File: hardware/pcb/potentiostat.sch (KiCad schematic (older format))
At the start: 58 parts

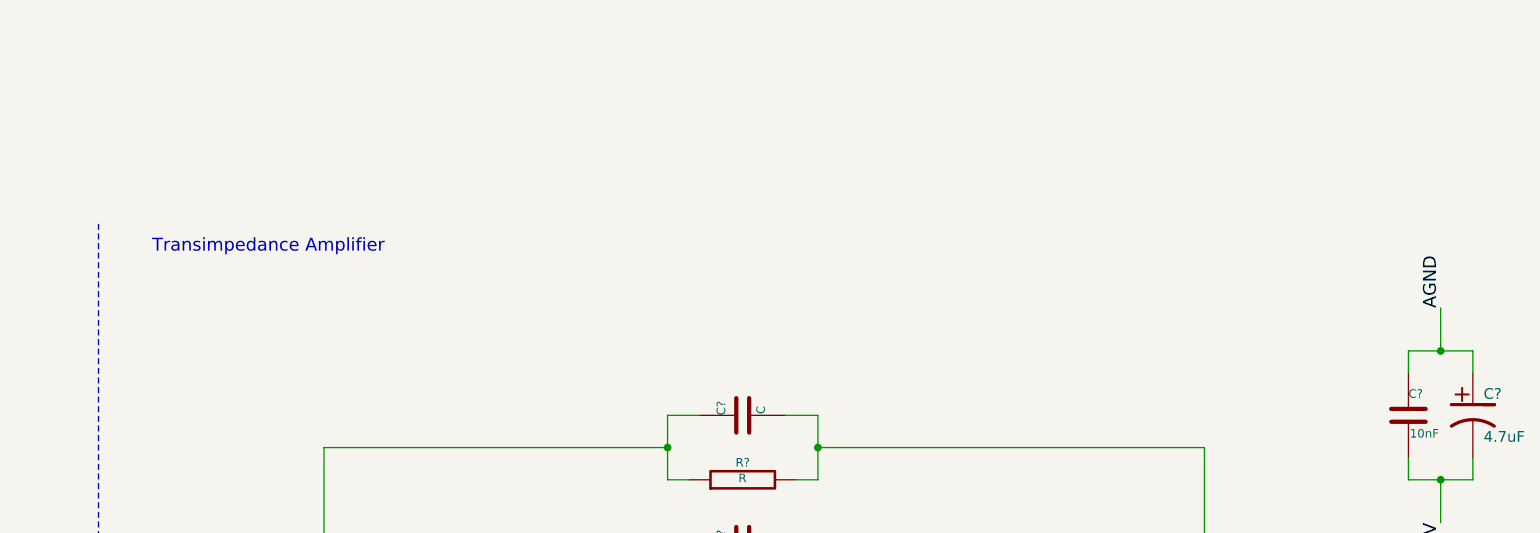
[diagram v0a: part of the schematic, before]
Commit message: Added note about switch arrangement.
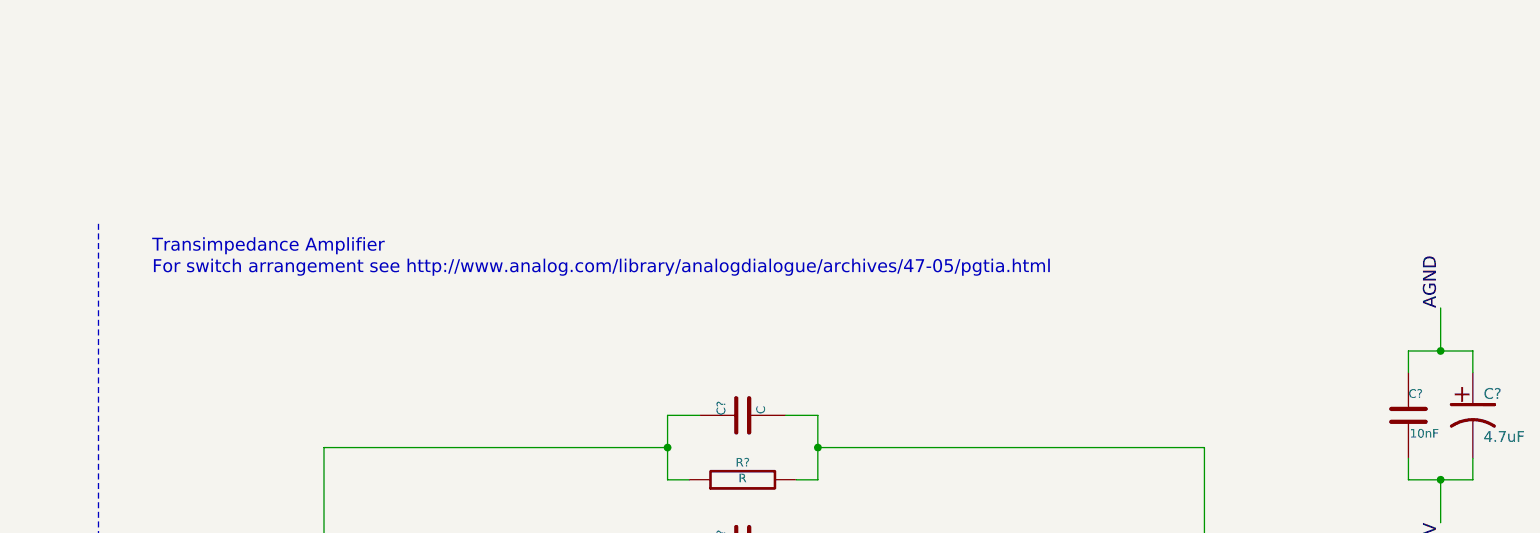
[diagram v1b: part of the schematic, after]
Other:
- note added: "For switch arrangement see http://www.analog.com/library/analogdialogue/archives/47-05/pgtia.html"
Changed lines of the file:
@@
 Sheet 1 1
 Title ""
-Date "17 may 2016"
+Date "19 may 2016"
 Rev ""
 Comp ""
@@
 Wire Wire Line
 	8500 11000 8300 11000
+Text Notes 6550 750  0    60   ~ 0
+For switch arrangement see http://www.analog.com/library/analogdialogue/archives/47-05/pgtia.html
 $EndSCHEMATC

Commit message: Worked on potentiostat design.
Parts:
- added P? (x12): CONN_2, symbol CONN_2
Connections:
- net +15V: now also P?.1 (P1), P?.2 (PM)
- net -15V: now also P?.1 (P1), P?.2 (PM)
- net AGND: now also P?.1 (P1), P?.2 (PM)
- net CTR_ELECT: now also P?.1 (P1), P?.2 (PM)
- net DAC_BIP: now also P?.1 (P1), P?.2 (PM)
- net DAC_BIP_NX: now also P?.1 (P1), P?.2 (PM)
- net DAC_UNI: now also P?.1 (P1), P?.2 (PM)
- net GND: now also P?.1 (P1), P?.2 (PM)
- net REF_0V6: now also P?.1 (P1), P?.2 (PM)
- net REF_ELECT_BUF: now also P?.1 (P1), P?.2 (PM)
- net TIA_OUT_BIP: now reaches U?.10 (M1), U?.11 (S3), U?.14 (S2), U?.3 (S1), U?.6 (S4)
- net TIA_OUT_BIP: now also P?.1 (P1), P?.2 (PM)
- net TIA_OUT renamed TIA_OUT_UNI
- net TIA_OUT_UNI: now also P?.1 (P1), P?.2 (PM)
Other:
- note added: "+/- 15V supply test points"
- note added: "0.6V ref. voltage test point"
- note added: "For switch arrangement see http://www.analog.com/library/analogdialogue/archives/47-05/pgtia.html\n\nSet gains so that output voltage range is -0.6V to 0.6V. \n\nInput current ranges (+/-) 1uA, 10uA, 100uA, 1000uA"
- note added: "GND test points"
- note added: "NX scaled DAC test point"
- note added: "bipolor/unipolar transimpedance \namplifier output test poinsts"
- note added: "buffered ref. electrode test point"
- note added: "couter electrode test point"
- note added: "unipolar/bipolar DAC test points"
- note removed: "For switch arrangement see http://www.analog.com/library/analogdialogue/archives/47-05/pgtia.html"
- moved on the sheet: C?, R?, U?

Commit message: Enlarged schematic sheet for addition of 10V reference and differential amplifier.
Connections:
- net SCL: now also U?.26 (D19,A5,SCL0,TOUCH); no longer U?.41 (SCL1,A18,D29)
- net SDA: now also U?.25 (D18,A4,SDA0,TOUCH); no longer U?.42 (SDA1,A19,D30)
- net REF_ELECT_UNI: now reaches U?.23 (D16,A2,TOUCH)
- no-connect marks 36 -> 33
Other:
- moved on the sheet: K?, P?, U?
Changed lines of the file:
@@
 EELAYER 27 0
 EELAYER END
-$Descr User 17000 14000
+$Descr User 17000 16500
 encoding utf-8
 Sheet 1 1
 Title ""
-Date "28 sep 2016"
+Date "29 sep 2016"
 Rev ""
 Comp ""
@@
 L MEA1D05XXSC U?
 U 1 1 573678C5
-P 6800 12475
-F 0 "U?" H 6800 12925 60  0000 C CNN
-F 1 "MEA1D05XXSC" H 6800 12025 60  0000 C CNN
-F 2 "~" H 6700 12375 60  0000 C CNN
-F 3 "~" H 6700 12375 60  0000 C CNN
-	1    6800 12475
-	1    0    0    -1
-$EndComp
-Text Label 7500 12625 0    60   ~ 0
+P 6900 14975
+F 0 "U?" H 6900 15425 60  0000 C CNN
+F 1 "MEA1D05XXSC" H 6900 14525 60  0000 C CNN
+F 2 "~" H 6800 14875 60  0000 C CNN
+F 3 "~" H 6800 14875 60  0000 C CNN
+	1    6900 14975
+	1    0    0    -1
+$EndComp
+Text Label 7600 15125 0    60   ~ 0
 GND
-NoConn ~ 7200 12425
-Text Label 7500 12525 0    60   ~ 0
+NoConn ~ 7300 14925
+Text Label 7600 15025 0    60   ~ 0
 -15V
-Text Label 7500 12725 0    60   ~ 0
+Text Label 7600 15225 0    60   ~ 0
 +15V
 Text Label 1800 3650 2    60   ~ 0
 5V
-Text Label 7500 12225 0    60   ~ 0
+Text Label 7600 14725 0    60   ~ 0
 5V
-Text Notes 6900 11650 0    60   ~ 0
+Text Notes 7000 14150 0    60   ~ 0
 +/- 15V Supply for OPAMPs
 $Comp
@@
 Connection ~ 12300 8225
 Wire Wire Line
-	7200 12325 7300 12325
-Wire Wire Line
-	7300 12325 7300 12625
-Wire Wire Line
-	7200 12625 7500 12625
-Connection ~ 7300 12625
-Wire Wire Line
-	7200 12525 7500 12525
-Wire Wire Line
-	7200 12725 7500 12725
-Wire Wire Line
-	7200 12225 7500 12225
+	7300 14825 7400 14825
+Wire Wire Line
+	7400 14825 7400 15125
+Wire Wire Line
+	7300 15125 7600 15125
+Connection ~ 7400 15125
+Wire Wire Line
+	7300 15025 7600 15025
+Wire Wire Line
+	7300 15225 7600 15225
+Wire Wire Line
+	7300 14725 7600 14725
 Wire Wire Line
 	2000 3650 1800 3650
@@
 L CONN_3 K?
 U 1 1 5737F060
-P 2250 12350
-F 0 "K?" V 2200 12350 50  0000 C CNN
-F 1 "CONN_3" V 2300 12350 40  0000 C CNN
-F 2 "" H 2250 12350 60  0000 C CNN
-F 3 "" H 2250 12350 60  0000 C CNN
-	1    2250 12350
-	1    0    0    -1
-$EndComp
-Wire Wire Line
-	1900 12250 1700 12250
-Wire Wire Line
-	1900 12350 1700 12350
-Wire Wire Line
-	1900 12450 1700 12450
-Text Label 1700 12350 2    60   ~ 0
+P 2350 14850
+F 0 "K?" V 2300 14850 50  0000 C CNN
+F 1 "CONN_3" V 2400 14850 40  0000 C CNN
+F 2 "" H 2350 14850 60  0000 C CNN
+F 3 "" H 2350 14850 60  0000 C CNN
+	1    2350 14850
+	1    0    0    -1
+$EndComp
+Wire Wire Line
+	2000 14750 1800 14750
+Wire Wire Line
+	2000 14850 1800 14850
+Wire Wire Line
+	2000 14950 1800 14950
+Text Label 1800 14850 2    60   ~ 0
 REF_ELECT
-Text Label 1700 12250 2    60   ~ 0
+Text Label 1800 14750 2    60   ~ 0
 CTR_ELECT
-Text Label 1700 12450 2    60   ~ 0
+Text Label 1800 14950 2    60   ~ 0
 WRK_ELECT
 Text Label 11050 4450 0    60   ~ 0
@@
 GND
 NoConn ~ 2000 2750
-NoConn ~ 2000 2850
-NoConn ~ 2000 2950
 NoConn ~ 2000 3050
 NoConn ~ 2000 3150
@@
 SCK
 Wire Wire Line
-	4050 2800 4250 2800
-Wire Wire Line
-	4050 2900 4250 2900
+	2000 2850 1800 2850
+Wire Wire Line
+	2000 2950 1800 2950
 NoConn ~ 4050 1950
-Text Label 4250 2800 0    60   ~ 0
+Text Label 1800 2850 2    60   ~ 0
 SDA
-Text Label 4250 2900 0    60   ~ 0
+Text Label 1800 2950 2    60   ~ 0
 SCL
 NoConn ~ 2000 3450
@@
 	1800 2550 2000 2550
 NoConn ~ 2000 2450
-NoConn ~ 2000 2650
 $Comp
 L CONN_5X2 P?
 U 1 1 57398AAE
-P 11350 12200
-F 0 "P?" H 11350 12500 60  0000 C CNN
-F 1 "CONN_5X2" V 11350 12200 50  0000 C CNN
-F 2 "" H 11350 12200 60  0000 C CNN
-F 3 "" H 11350 12200 60  0000 C CNN
-	1    11350 12200
-	1    0    0    -1
-$EndComp
-Wire Wire Line
-	10950 12000 10750 12000
-Wire Wire Line
-	10750 12100 10950 12100
-Wire Wire Line
-	10950 12200 10750 12200
-Wire Wire Line
-	10950 12300 10750 12300
-Wire Wire Line
-	10950 12400 10750 12400
-Wire Wire Line
-	11750 12000 11950 12000
-Wire Wire Line
-	11750 12100 11950 12100
-Wire Wire Line
-	11750 12200 11950 12200
-Wire Wire Line
-	11750 12300 11950 12300
-Wire Wire Line
-	11750 12400 11950 12400
-Text Label 10750 12000 2    60   ~ 0
+P 11450 14700
+F 0 "P?" H 11450 15000 60  0000 C CNN
+F 1 "CONN_5X2" V 11450 14700 50  0000 C CNN
+F 2 "" H 11450 14700 60  0000 C CNN
+F 3 "" H 11450 14700 60  0000 C CNN
+	1    11450 14700
+	1    0    0    -1
+$EndComp
+Wire Wire Line
+	11050 14500 10850 14500
+Wire Wire Line
+	10850 14600 11050 14600
+Wire Wire Line
+	11050 14700 10850 14700
+Wire Wire Line
+	11050 14800 10850 14800
+Wire Wire Line
+	11050 14900 10850 14900
+Wire Wire Line
+	11850 14500 12050 14500
+Wire Wire Line
+	11850 14600 12050 14600
+Wire Wire Line
+	11850 14700 12050 14700
+Wire Wire Line
+	11850 14800 12050 14800
+Wire Wire Line
+	11850 14900 12050 14900
+Text Label 10850 14500 2    60   ~ 0
 VUEXT
-Text Label 11950 12000 0    60   ~ 0
+Text Label 12050 14500 0    60   ~ 0
 GND
-Text Label 10750 12100 2    60   ~ 0
+Text Label 10850 14600 2    60   ~ 0
 TX
-Text Label 11950 12100 0    60   ~ 0
+Text Label 12050 14600 0    60   ~ 0
 RX
-Text Label 10750 12200 2    60   ~ 0
+Text Label 10850 14700 2    60   ~ 0
 SCL
-Text Label 11950 12200 0    60   ~ 0
+Text Label 12050 14700 0    60   ~ 0
 SDA
-Text Label 10750 12300 2    60   ~ 0
+Text Label 10850 14800 2    60   ~ 0
 MISO
-Text Label 11950 12300 0    60   ~ 0
+Text Label 12050 14800 0    60   ~ 0
 MOSI
-Text Label 10750 12400 2    60   ~ 0
+Text Label 10850 14900 2    60   ~ 0
 SCK
-Text Label 11950 12400 0    60   ~ 0
+Text Label 12050 14900 0    60   ~ 0
 CS
-Text Notes 10750 11650 0    60   ~ 0
+Text Notes 10850 14150 0    60   ~ 0
 UEXT EXPANSION HEADER
 $Comp
 L CONN_2X2 P?
 U 1 1 573999BF
-P 14750 12150
-F 0 "P?" H 14750 12300 50  0000 C CNN
-F 1 "CONN_2X2" H 14760 12020 40  0000 C CNN
-F 2 "" H 14750 12150 60  0000 C CNN
-F 3 "" H 14750 12150 60  0000 C CNN
-	1    14750 12150
-	1    0    0    -1
-$EndComp
-Wire Wire Line
-	15150 12100 15250 12100
-Wire Wire Line
-	15250 12100 15250 12200
-Wire Wire Line
-	15250 12200 15150 12200
-Wire Wire Line
-	15250 12150 15450 12150
-Connection ~ 15250 12150
-Wire Wire Line
-	14350 12100 14150 12100
-Wire Wire Line
-	14150 12200 14350 12200
-Text Label 14150 12100 2    60   ~ 0
+P 14850 14650
+F 0 "P?" H 14850 14800 50  0000 C CNN
+F 1 "CONN_2X2" H 14860 14520 40  0000 C CNN
+F 2 "" H 14850 14650 60  0000 C CNN
+F 3 "" H 14850 14650 60  0000 C CNN
+	1    14850 14650
+	1    0    0    -1
+$EndComp
+Wire Wire Line
+	15250 14600 15350 14600
+Wire Wire Line
+	15350 14600 15350 14700
+Wire Wire Line
+	15350 14700 15250 14700
+Wire Wire Line
+	15350 14650 15550 14650
+Connection ~ 15350 14650
+Wire Wire Line
+	14450 14600 14250 14600
+Wire Wire Line
+	14250 14700 14450 14700
+Text Label 14250 14600 2    60   ~ 0
 5V
-Text Label 14150 12200 2    60   ~ 0
+Text Label 14250 14700 2    60   ~ 0
 3V3
-Text Label 15450 12150 0    60   ~ 0
+Text Label 15550 14650 0    60   ~ 0
 VUEXT
-Text Notes 14350 11650 0    60   ~ 0
+Text Notes 14450 14150 0    60   ~ 0
 UEXT POWER SELECT
-Text Notes 650  11650 0    60   ~ 0
+Text Notes 750  14150 0    60   ~ 0
 Electrode Connector
 $Comp
@@
 	6300 9250 6300 11450
 Wire Notes Line
-	6300 11550 6300 13450
+	6300 14050 6300 15950
 Text Notes 350  -2700 0    200  ~ 40
 Notes:
@@
 5. Specify missing component values e.g. transimpedance amplifier Rs and Cs.
 Wire Notes Line
-	450  6800 350  6800
-Wire Notes Line
-	450  9200 350  9200
-Wire Notes Line
-	450  11500 300  11500
-Wire Notes Line
 	500  6800 16500 6800
 Wire Notes Line
@@
 	500  4600 6250 4600
 Wire Notes Line
-	9350 11550 9350 13500
+	9450 14050 9450 16000
 Wire Notes Line
-	13250 11550 13250 12900
+	13350 14050 13350 15400
 $Comp
 L C C?
@@
 L CONN_2 P?
 U 1 1 57EC2AB5
-P 8950 11900
-F 0 "P?" V 8900 11900 40  0000 C CNN
-F 1 "CONN_2" V 9000 11900 40  0000 C CNN
-F 2 "" H 8950 11900 60  0000 C CNN
-F 3 "" H 8950 11900 60  0000 C CNN
-	1    8950 11900
-	0    -1   -1   0
-$EndComp
-Wire Wire Line
-	8850 12250 8850 12350
-Wire Wire Line
-	8600 12350 9050 12350
-Wire Wire Line
-	9050 12350 9050 12250
-Connection ~ 8850 12350
-Text Label 8600 12350 2    60   ~ 0
+P 9050 14400
+F 0 "P?" V 9000 14400 40  0000 C CNN
+F 1 "CONN_2" V 9100 14400 40  0000 C CNN
+F 2 "" H 9050 14400 60  0000 C CNN
+F 3 "" H 9050 14400 60  0000 C CNN
+	1    9050 14400
+	0    -1   -1   0
+$EndComp
+Wire Wire Line
+	8950 14750 8950 14850
+Wire Wire Line
+	8700 14850 9150 14850
+Wire Wire Line
+	9150 14850 9150 14750
+Connection ~ 8950 14850
+Text Label 8700 14850 2    60   ~ 0
 -15V
 $Comp
 L CONN_2 P?
 U 1 1 57EC2AC0
-P 8950 12650
-F 0 "P?" V 8900 12650 40  0000 C CNN
-F 1 "CONN_2" V 9000 12650 40  0000 C CNN
-F 2 "" H 8950 12650 60  0000 C CNN
-F 3 "" H 8950 12650 60  0000 C CNN
-	1    8950 12650
-	0    -1   -1   0
-$EndComp
-Wire Wire Line
-	8850 13000 8850 13100
-Wire Wire Line
-	8600 13100 9050 13100
-Wire Wire Line
-	9050 13100 9050 13000
-Connection ~ 8850 13100
-Text Label 8600 13100 2    60   ~ 0
+P 9050 15150
+F 0 "P?" V 9000 15150 40  0000 C CNN
+F 1 "CONN_2" V 9100 15150 40  0000 C CNN
+F 2 "" H 9050 15150 60  0000 C CNN
+F 3 "" H 9050 15150 60  0000 C CNN
+	1    9050 15150
+	0    -1   -1   0
+$EndComp
+Wire Wire Line
+	8950 15500 8950 15600
+Wire Wire Line
+	8700 15600 9150 15600
+Wire Wire Line
+	9150 15600 9150 15500
+Connection ~ 8950 15600
+Text Label 8700 15600 2    60   ~ 0
 +15V
-Text Notes 7900 13350 0    60   ~ 0
+Text Notes 8000 15850 0    60   ~ 0
 +/- 15V supply test points
 $Comp
@@
 Text Notes 15200 11350 0    60   ~ 0
 couter electrode test point
+Wire Wire Line
+	2000 2650 1800 2650
+Text Label 1800 2650 2    60   ~ 0
+REF_ELECT_UNI
+Wire Notes Line
+	500  14000 16500 14000
+Wire Notes Line
+	6300 11550 6300 13950
 $EndSCHEMATC

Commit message: Finished initial schematic layout. Component values assigned. Passes DRC.
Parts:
- removed K?: CONN_3, symbol CONN_3
- added C10, C12, C13, C14: 0.1uF, ~, symbol C
- added D1: BAS07-04, ~, symbol BAS07-04
- added P1, P18, P2, P3, P8: CONN_2, symbol CONN_2
- added R10, R11, R9: 50k, ~, symbol R
- added R12, R13: 3k, ~, symbol R
- added R14: 1k, ~, symbol R
- added R15: 100, ~, symbol R
- added R4: 191, ~, symbol R
- added U11: OP07, ~, symbol OP07
- added U3: MAX6176AASA+, ~, symbol MAX6176AASA+
- C19, C20: renamed from C?; value C -> 56
- C21, C22: renamed from C?; value C -> 56nF
- C23, C24, C33, C35: renamed from C?; value C -> 0.1uF
- R16: renamed from R?; value R -> 1k
- R17: renamed from R?; value R -> 100
- R2, R3: renamed from R?; value R -> 10k
- R5: renamed from R?; value R -> 600
- R6: renamed from R?; value R -> 6k
- R7: renamed from R?; value R -> 60k
- R8: renamed from R?; value R -> 600k
- gave numbers to parts that had none: 53
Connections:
- net -12V is gone; now on net -15V: U5.6 (~WR)
- net +15V: now also C13.1, U11.7 (V+)
- net -15V: now also C14.1, U11.4 (V-)
- net 3V3: now also D1.2 (cathode)
- net 5V: now also C12.1
- net AGND: now also C13.2, C14.2, D1.1 (Anode), P1.2 (PM), P2.2 (PM), P3.2 (PM), R4.1, R9.1
- net CTR_ELECT: now also P1.1 (P1), P18.1 (P1), P18.2 (PM)
- net GND: now also C10.2, C12.2, U3.4 (GND)
- net REF_0V6: now also P8.1 (P1), P8.2 (PM)
- net REF_ELECT: now also P2.1 (P1)
- net REF_ELECT_BUF: now also R3.2, R10.1; no longer R3.1
- net REF_ELECT_UNI: now also R15.2
- net WRK_ELECT: now also P3.1 (P1)
- net at R2.2, U10.2 (IN-): now also R3.1; no longer R3.2
- new net: R13.1, R9.2, U11.2 (-IN)
- new net: R10.2, R11.2, R12.2, U11.3 (+IN)
- new net: R13.2, R14.1, U11.6 (OUT)
- new net: D1.3 (AK), R14.2, R15.1
- new net: R12.1, R4.2
- new net 10V_REF: R11.1, U3.6 (OUT)
- new net 15V: C10.1, U3.2 (IN)
- no-connect marks 33 -> 43
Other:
- note added: "10V Reference voltage."
- note added: "10V ref. voltage test point"
- note added: "Differential Amplifier - shifts and scales +/- 10V REF_ELECT_BUF into 0-1.2V range for analog input."
- note added: "For switch arrangement see http://www.analog.com/library/analogdialogue/archives/47-05/pgtia.html\n\nSet gains so that output voltage range is -0.6V to 0.6V. \n\nInput current ranges (+/-) 1uA, 10uA, 100uA, 1000uA \n\nC values - may need tobe refined"
- note added: "counter electrode test point"
- note added: "unipolar ref. electrode test point"
- note removed: "1. Add analog input for reference electrode (buffered). Could just take -[10V, 10V] analog input from noah motion controller."
- note removed: "2. Add test points for debugging?"
- note removed: "3. Edit library pin definitions to so that DRC works correctly."
- note removed: "4. Add power flags for DRC works correctly."
- note removed: "5. Specify missing component values e.g. transimpedance amplifier Rs and Cs."
- note removed: "For switch arrangement see http://www.analog.com/library/analogdialogue/archives/47-05/pgtia.html\n\nSet gains so that output voltage range is -0.6V to 0.6V. \n\nInput current ranges (+/-) 1uA, 10uA, 100uA, 1000uA"
- note removed: "Notes:"
- note removed: "couter electrode test point"
- moved on the sheet: C15, C16, C17, C18, C23, C24, C33, C35, P11, P12, P19, U6

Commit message: Added second optional expasion header, i2c pullups and 2nd electrode connector.
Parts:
- added K1: CONN_3, symbol CONN_3
- added P14: CONN_5X2, symbol CONN_5X2
- added P16: CONN_2X2, symbol CONN_2X2
- added R14, R16: R, ~, symbol R
- renumbered P14 to P15, P15 to P17, P16 to P18, P17 to P19, P18 to P20, P19 to P21, R14 to R15, R15 to R17, R16 to R18, R17 to R19
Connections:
- net 3V3: now also P16.3
- net 5V: now also P16.1
- net CTR_ELECT: now also K1.1 (P1)
- net GND: now also P14.2
- net REF_ELECT: now also K1.2 (PM)
- net SCL: now also R14.2
- net SDA: now also R16.2
- net VUEXT: now also R14.1, R16.1
- net WRK_ELECT: now also K1.3 (P3)
- net D24: now reaches U2.36 (D24)
- net D24: now also P14.3
- net D25: now reaches U2.37 (TOUCH,PWM,D25)
- net D25: now also P14.4
- net D26: now reaches U2.38 (A15,D26)
- net D26: now also P14.5
- net D27: now reaches U2.39 (A16,D27)
- net D27: now also P14.6
- net D28: now reaches U2.40 (A17,D28)
- net D28: now also P14.7
- net D29: now reaches U2.41 (SCL1,A18,D29)
- net D29: now also P14.8
- net D30: now reaches U2.42 (SDA1,A19,D30)
- net D30: now also P14.9
- net D31: now reaches U2.43 (A20,D31)
- net D31: now also P14.10
- new net VEXP: P14.1, P16.2, P16.4
- no-connect marks 43 -> 35
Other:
- note added: "Electrode Connectors"
- note added: "Expansion header power selection"
- note added: "Expanson Headers"
- note removed: "Electrode Connector"
- note removed: "UEXT EXPANSION HEADER"
- note removed: "UEXT POWER SELECT"
- moved on the sheet: P1, P13, P15, P2, P3

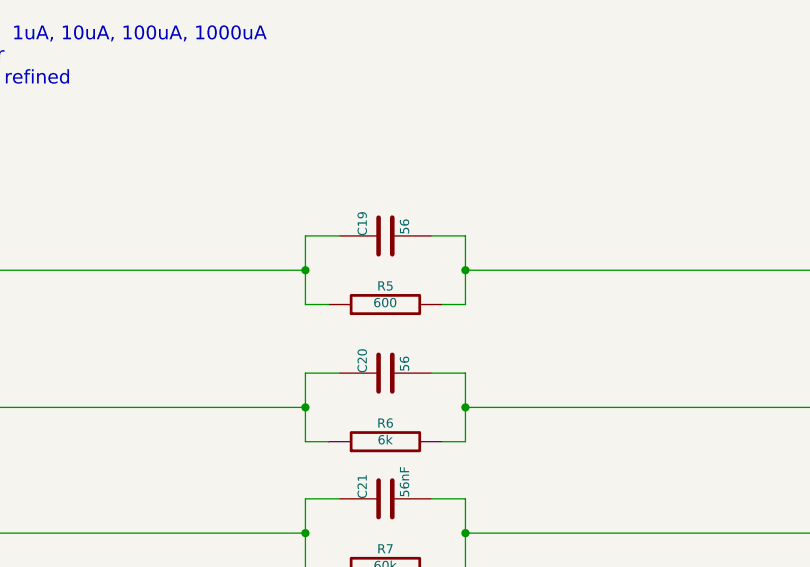
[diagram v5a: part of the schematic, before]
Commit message: Worked on footprint assignments.
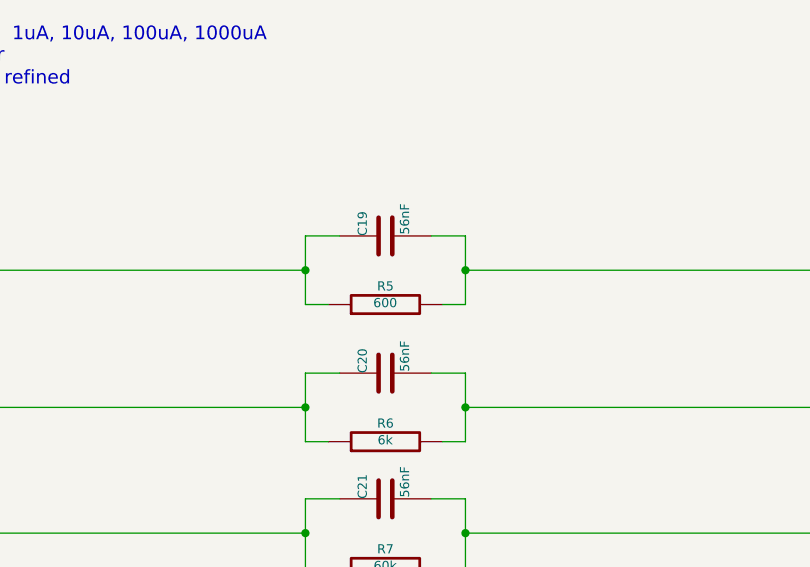
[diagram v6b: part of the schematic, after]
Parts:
- C19, C20: value 56 -> 56nF
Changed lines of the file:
@@
 P 9300 2000
 F 0 "C20" H 9300 2100 40  0000 L CNN
-F 1 "56" H 9306 1915 40  0000 L CNN
+F 1 "56nF" H 9306 1915 40  0000 L CNN
 F 2 "~" H 9338 1850 30  0000 C CNN
 F 3 "~" H 9300 2000 60  0000 C CNN
@@
 P 9300 1400
 F 0 "C19" H 9300 1500 40  0000 L CNN
-F 1 "56" H 9306 1315 40  0000 L CNN
+F 1 "56nF" H 9306 1315 40  0000 L CNN
 F 2 "~" H 9338 1250 30  0000 C CNN
 F 3 "~" H 9300 1400 60  0000 C CNN

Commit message: Worked on footprint assignment.
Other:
- note added: "Use ADG441"
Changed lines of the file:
@@
 Sheet 1 1
 Title ""
-Date "30 sep 2016"
+Date "16 nov 2016"
 Rev ""
 Comp ""
@@
 Text Label 4150 15150 2    60   ~ 0
 WRK_ELECT
+Text Notes 11150 4900 0    60   ~ 0
+Use ADG441
 $EndSCHEMATC
